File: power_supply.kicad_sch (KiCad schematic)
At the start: 21 parts, among them U3 TPS62913, U4 TPS7A4701RGWR, U5 LDL1117S33R

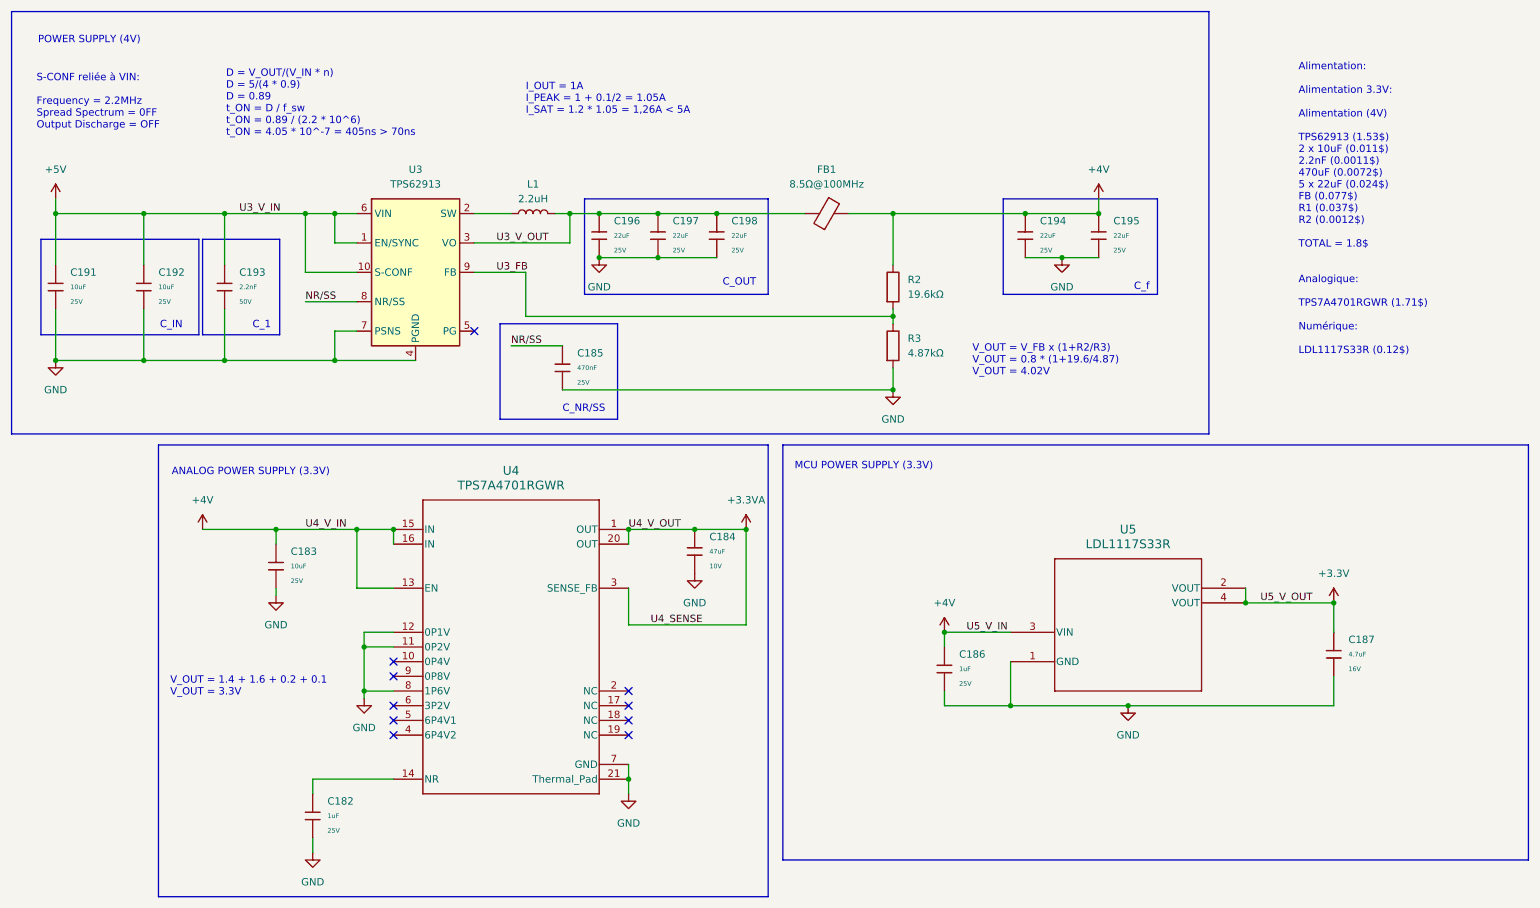
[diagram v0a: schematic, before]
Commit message: start analog ldo layout
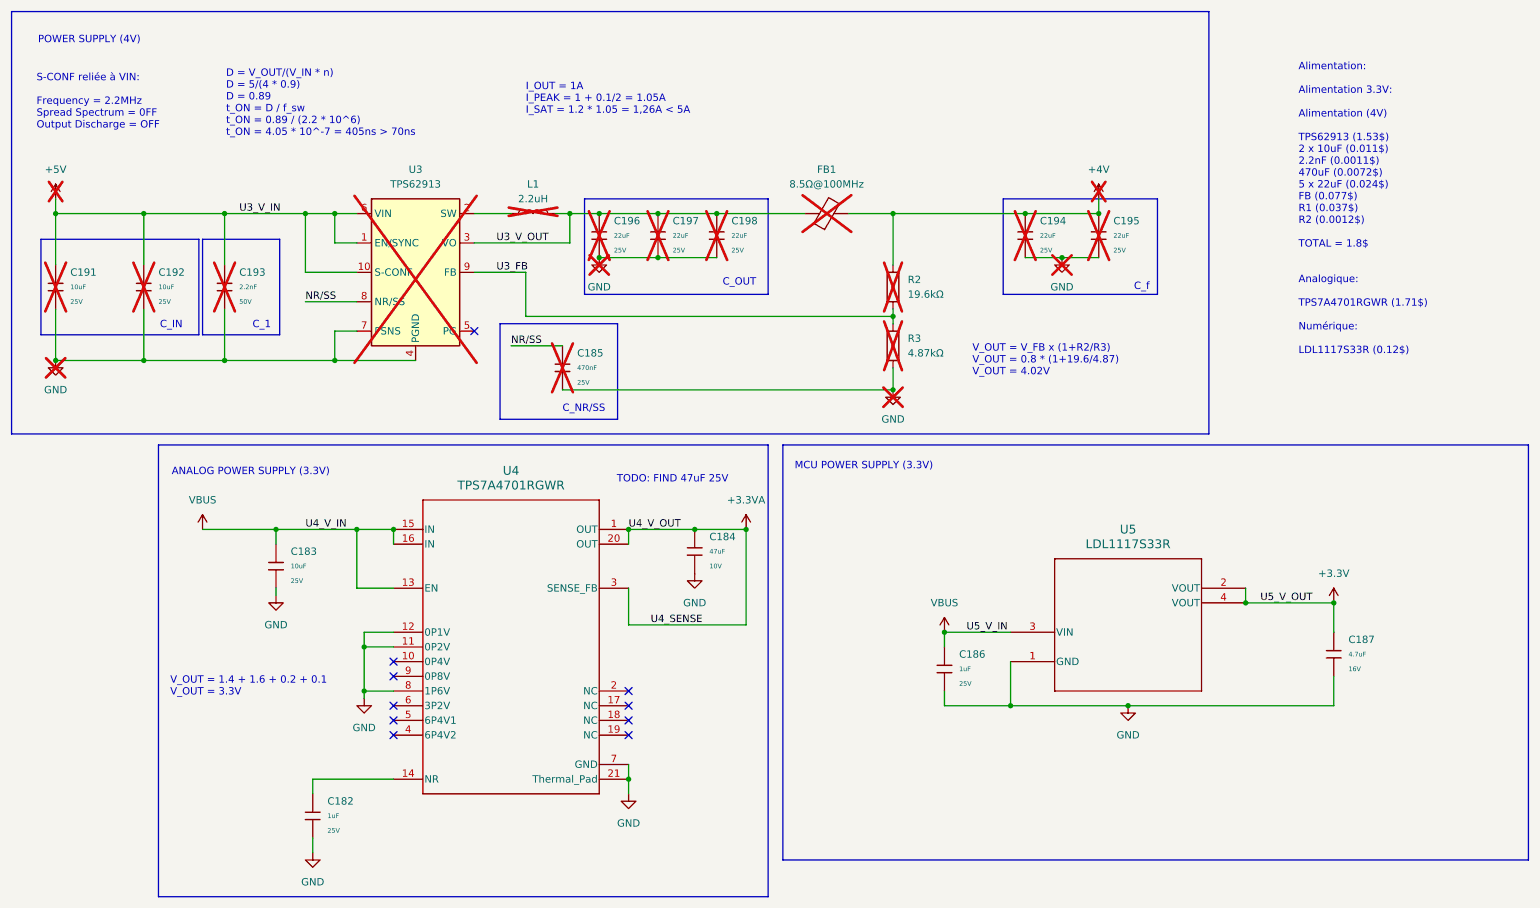
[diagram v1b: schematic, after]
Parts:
- C185, C191, C192, C193, C194, C195, C196, C197, C198, FB1, L1, R2, R3, U3: now not fitted; now left out of the parts list
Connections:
- net +4V: no longer C183.1, C186.1, U4.13 (EN), U4.15 (IN), U4.16 (IN), U5.3 (VIN)
- new net VBUS: C183.1, C186.1, U4.13 (EN), U4.15 (IN), U4.16 (IN), U5.3 (VIN)
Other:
- note added: "TODO: FIND 47uF 25V"

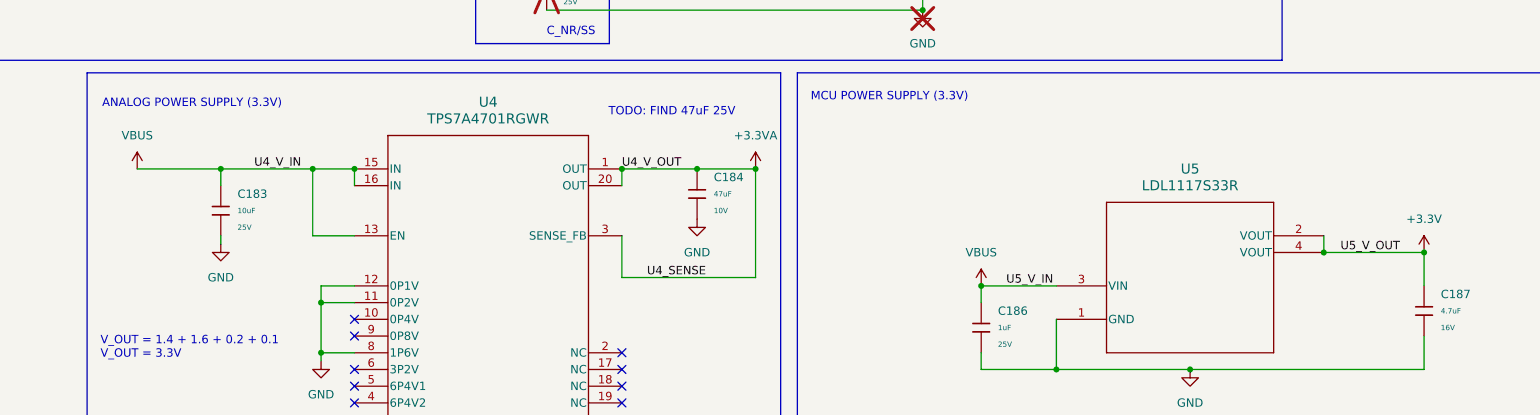
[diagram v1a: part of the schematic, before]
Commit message: vdda power supply & sensor decoupling capacitor
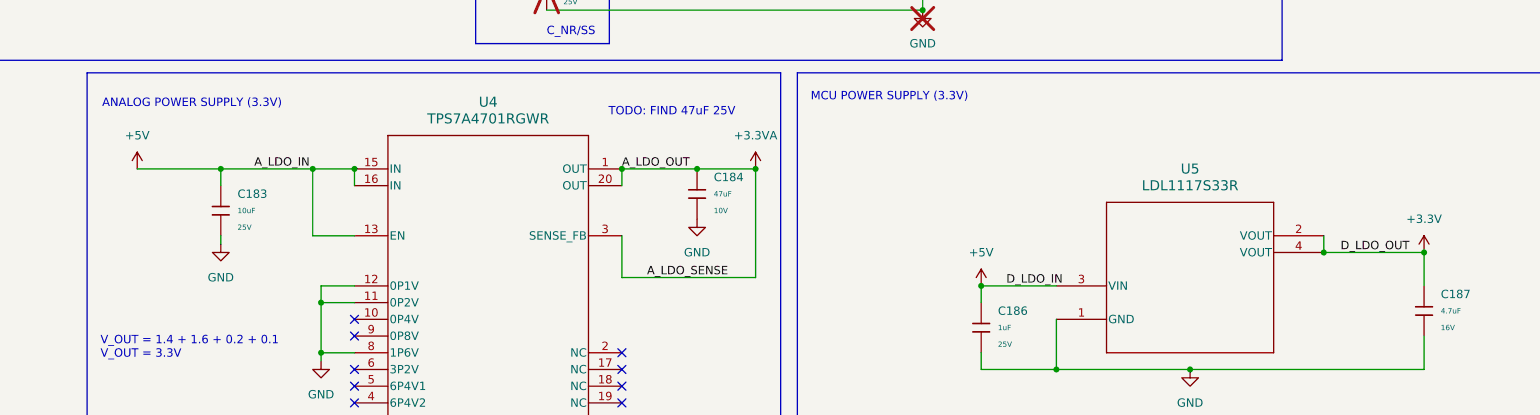
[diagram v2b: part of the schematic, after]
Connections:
- net VBUS is gone; now on net +5V: C183.1, C186.1, U4.13 (EN), U4.15 (IN), U4.16 (IN), U5.3 (VIN)
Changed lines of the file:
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@@
-	)
-	(junction
-		(at 177.8 124.46)
-		(diameter 0)
-		(color 0 0 0 0)
 	)
 	(junction
@@
 	(junction
 		(at 128.27 52.07)
+		(diameter 0)
+		(color 0 0 0 0)
+	)
+	(junction
+		(at 177.8 124.46)
 		(diameter 0)
 		(color 0 0 0 0)
@@
 		)
 	)
-	(label "U4_V_OUT"
+	(label "A_LDO_OUT"
 		(at 123.19 106.68 0)
 		(effects
@@
 		)
 	)
-	(label "U4_V_IN"
+	(label "A_LDO_IN"
 		(at 67.31 106.68 0)
 		(effects
@@
 		)
 	)
-	(label "U4_SENSE"
+	(label "A_LDO_SENSE"
 		(at 127 123.19 0)
 		(effects
@@
 		)
 	)
-	(label "U5_V_OUT"
+	(label "D_LDO_OUT"
 		(at 232.41 119.38 0)
 		(effects
@@
 		)
 	)
-	(label "U5_V_IN"
+	(label "D_LDO_IN"
 		(at 181.61 124.46 0)
 		(effects
@@
 			)
 			(justify left bottom)
-		)
-	)
-	(symbol
-		(lib_id "power:VBUS")
-		(at 177.8 124.46 0)
-		(unit 1)
-		(exclude_from_sim no)
-		(in_bom yes)
-		(on_board yes)
-		(dnp no)
-		(fields_autoplaced yes)
-		(property "Reference" "#PWR0224"
-			(at 177.8 128.27 0)
-			(effects
-				(font
-					(size 1.27 1.27)
-				)
-				(hide yes)
-			)
-		)
-		(property "Value" "VBUS"
-			(at 177.8 119.38 0)
-			(effects
-				(font
-					(size 1.27 1.27)
-				)
-			)
-		)
-		(property "Footprint" ""
-			(at 177.8 124.46 0)
-			(effects
-				(font
-					(size 1.27 1.27)
-				)
-				(hide yes)
-			)
-		)
-		(property "Datasheet" ""
-			(at 177.8 124.46 0)
-			(effects
-				(font
-					(size 1.27 1.27)
-				)
-				(hide yes)
-			)
-		)
-		(property "Description" "Power symbol creates a global label with name \"VBUS\""
-			(at 177.8 124.46 0)
-			(effects
-				(font
-					(size 1.27 1.27)
-				)
-				(hide yes)
-			)
-		)
-		(pin "1"
-		)
-		(instances
-			(project "75he"
-				(path "/0edb4e17-93a4-4f7b-ad91-3a5c72b69d23/f26c38a6-65b7-4d4b-b531-bf41915dd707"
-					(reference "#PWR0224")
-					(unit 1)
-				)
-			)
 		)
 	)
@@
 	)
 	(symbol
+		(lib_id "power:+5V")
+		(at 177.8 124.46 0)
+		(unit 1)
+		(exclude_from_sim no)
+		(in_bom yes)
+		(on_board yes)
+		(dnp no)
+		(fields_autoplaced yes)
+		(property "Reference" "#PWR0223"
+			(at 177.8 128.27 0)
+			(effects
+				(font
+					(size 1.27 1.27)
+				)
+				(hide yes)
+			)
+		)
+		(property "Value" "+5V"
+			(at 177.8 119.38 0)
+			(effects
+				(font
+					(size 1.27 1.27)
+				)
+			)
+		)
+		(property "Footprint" ""
+			(at 177.8 124.46 0)
+			(effects
+				(font
+					(size 1.27 1.27)
+				)
+				(hide yes)
+			)
+		)
+		(property "Datasheet" ""
+			(at 177.8 124.46 0)
+			(effects
+				(font
+					(size 1.27 1.27)
+				)
+				(hide yes)
+			)
+		)
+		(property "Description" "Power symbol creates a global label with name \"+5V\""
+			(at 177.8 124.46 0)
+			(effects
+				(font
+					(size 1.27 1.27)
+				)
+				(hide yes)
+			)
+		)
+		(pin "1"
+		)
+		(instances
+			(project ""
+				(path "/0edb4e17-93a4-4f7b-ad91-3a5c72b69d23/f26c38a6-65b7-4d4b-b531-bf41915dd707"
+					(reference "#PWR0223")
+					(unit 1)
+				)
+			)
+		)
+	)
+	(symbol
 		(lib_id "Device:R")
 		(at 168.91 74.93 0)
@@
 	)
 	(symbol
+		(lib_id "power:+5V")
+		(at 49.53 106.68 0)
+		(unit 1)
+		(exclude_from_sim no)
+		(in_bom yes)
+		(on_board yes)
+		(dnp no)
+		(fields_autoplaced yes)
+		(property "Reference" "#PWR0221"
+			(at 49.53 110.49 0)
+			(effects
+				(font
+					(size 1.27 1.27)
+				)
+				(hide yes)
+			)
+		)
+		(property "Value" "+5V"
+			(at 49.53 101.6 0)
+			(effects
+				(font
+					(size 1.27 1.27)
+				)
+			)
+		)
+		(property "Footprint" ""
+			(at 49.53 106.68 0)
+			(effects
+				(font
+					(size 1.27 1.27)
+				)
+				(hide yes)
+			)
+		)
+		(property "Datasheet" ""
+			(at 49.53 106.68 0)
+			(effects
+				(font
+					(size 1.27 1.27)
+				)
+				(hide yes)
+			)
+		)
+		(property "Description" "Power symbol creates a global label with name \"+5V\""
+			(at 49.53 106.68 0)
+			(effects
+				(font
+					(size 1.27 1.27)
+				)
+				(hide yes)
+			)
+		)
+		(pin "1"
+		)
+		(instances
+			(project ""
+				(path "/0edb4e17-93a4-4f7b-ad91-3a5c72b69d23/f26c38a6-65b7-4d4b-b531-bf41915dd707"
+					(reference "#PWR0221")
+					(unit 1)
+				)
+			)
+		)
+	)
+	(symbol
 		(lib_id "Device:L")
 		(at 106.68 52.07 90)
@@
 					(unit 1)
 				)
-			)
-		)
-	)
-	(symbol
-		(lib_id "power:VBUS")
-		(at 49.53 106.68 0)
-		(unit 1)
-		(exclude_from_sim no)
-		(in_bom yes)
-		(on_board yes)
-		(dnp no)
-		(fields_autoplaced yes)
-		(property "Reference" "#PWR0223"
-			(at 49.53 110.49 0)
-			(effects
-				(font
-					(size 1.27 1.27)
-				)
-				(hide yes)
-			)
-		)
-		(property "Value" "VBUS"
-			(at 49.53 101.6 0)
-			(effects
-				(font
-					(size 1.27 1.27)
-				)
-			)
-		)
-		(property "Footprint" ""
-			(at 49.53 106.68 0)
-			(effects
-				(font
-					(size 1.27 1.27)
-				)
-				(hide yes)
-			)
-		)
-		(property "Datasheet" ""
-			(at 49.53 106.68 0)
-			(effects
-				(font
-					(size 1.27 1.27)
-				)
-				(hide yes)
-			)
-		)
-		(property "Description" "Power symbol creates a global label with name \"VBUS\""
-			(at 49.53 106.68 0)
-			(effects
-				(font
-					(size 1.27 1.27)
-				)
-				(hide yes)
-			)
-		)
-		(pin "1"
-		)
-		(instances
-			(project ""
-				(path "/0edb4e17-93a4-4f7b-ad91-3a5c72b69d23/f26c38a6-65b7-4d4b-b531-bf41915dd707"
-					(reference "#PWR0223")
-					(unit 1)
-				)

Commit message: caca
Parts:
- removed C185: 470nF, PCM_JLCPCB:C_0603, symbol PCM_JLCPCB-Capacitors:0603,470nF
- removed C191, C192: 10uF, PCM_JLCPCB:C_0805, symbol PCM_JLCPCB-Capacitors:0805,10uF
- removed C193: 2.2nF, PCM_JLCPCB:C_0402, symbol PCM_JLCPCB-Capacitors:0402,2.2nF
- removed C194, C195, C196, C197, C198: 22uF, PCM_JLCPCB:C_0805, symbol PCM_JLCPCB-Capacitors:0805,22uF
- removed FB1: 8.5Ω@100MHz, PCM_JLCPCB:FB_0603, symbol Device:FerriteBead
- removed L1: 2.2uH, Inductor_SMD:L_1210_3225Metric, symbol Device:L
- removed R2: 19.6kΩ, Resistor_SMD:R_0402_1005Metric, symbol Device:R
- removed R3: 4.87kΩ, PCM_JLCPCB:R_0603, symbol Device:R
- removed U3: TPS62913, Package_DFN_QFN:Texas_RPU0010A_VQFN-HR-10_2x2mm_P0.5mm, symbol Regulator_Switching:TPS62913
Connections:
- no-connect marks 10 -> 9
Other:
- note removed: "C_1"
- note removed: "C_IN"
- note removed: "C_NR/SS"
- note removed: "C_OUT"
- note removed: "C_f"
- note removed: "D = V_OUT/(V_IN * n) D = 5/(4 * 0.9) D = 0.89 t_ON = D / f_sw t_ON = 0.89 / (2.2 * 10^6) t_ON = 4.05 * 10^-7 = 405ns > 70ns"
- note removed: "I_OUT = 1A I_PEAK = 1 + 0.1/2 = 1.05A I_SAT = 1.2 * 1.05 = 1,26A < 5A"
- note removed: "POWER SUPPLY (4V)"
- note removed: "S-CONF reliée à VIN: Frequency = 2.2MHz Spread Spectrum = 0FF Output Discharge = OFF"
- note removed: "V_OUT = V_FB x (1+R2/R3) V_OUT = 0.8 * (1+19.6/4.87) V_OUT = 4.02V"

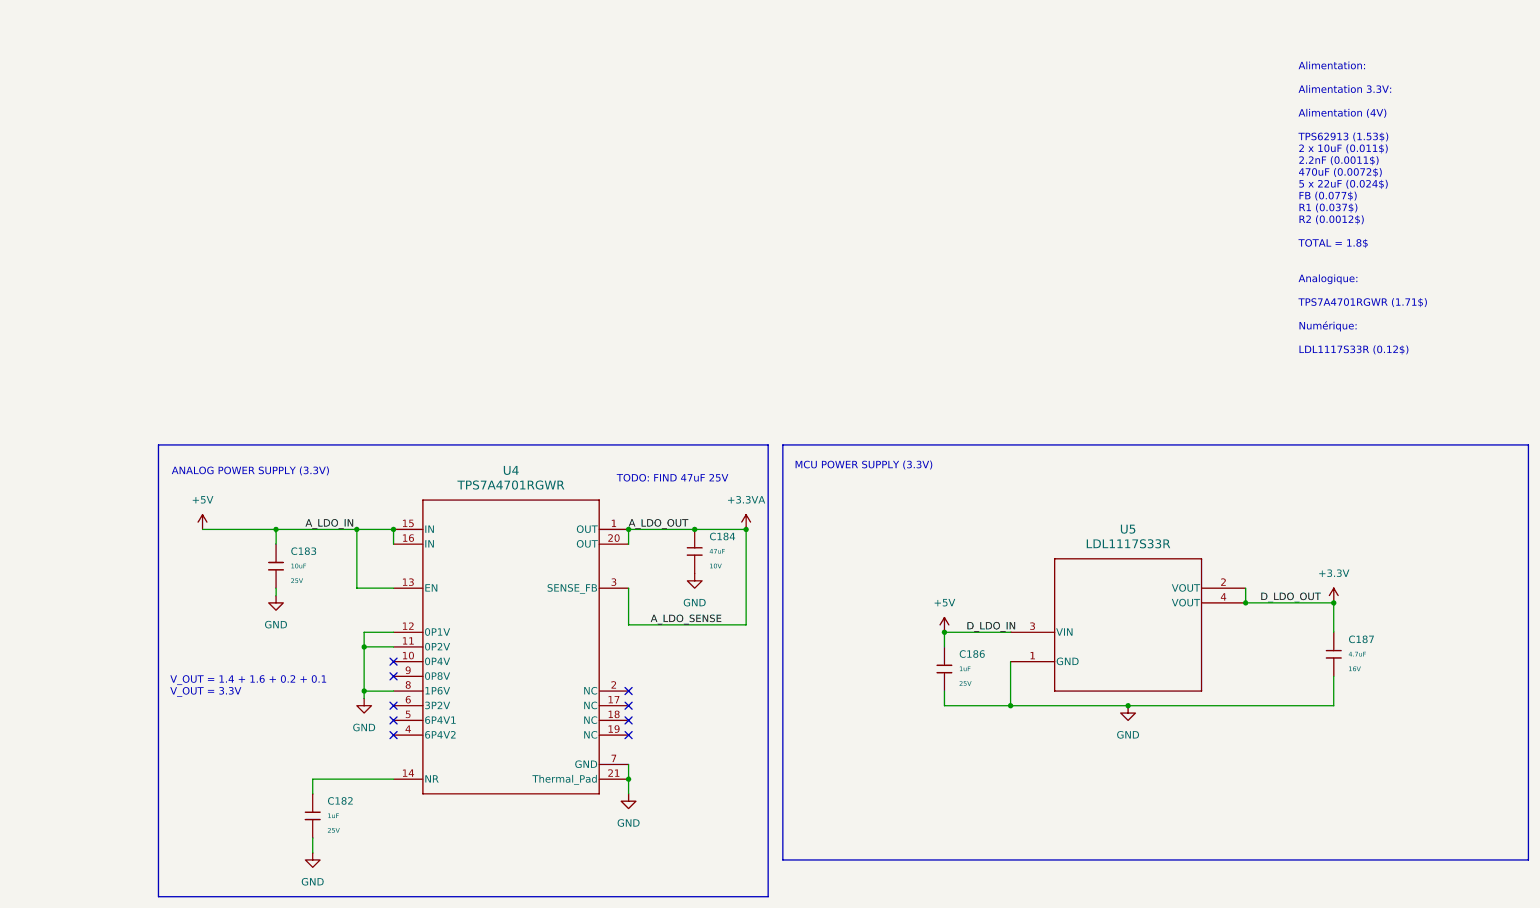
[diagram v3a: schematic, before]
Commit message: added power led, some cleanup/fixes, added doc
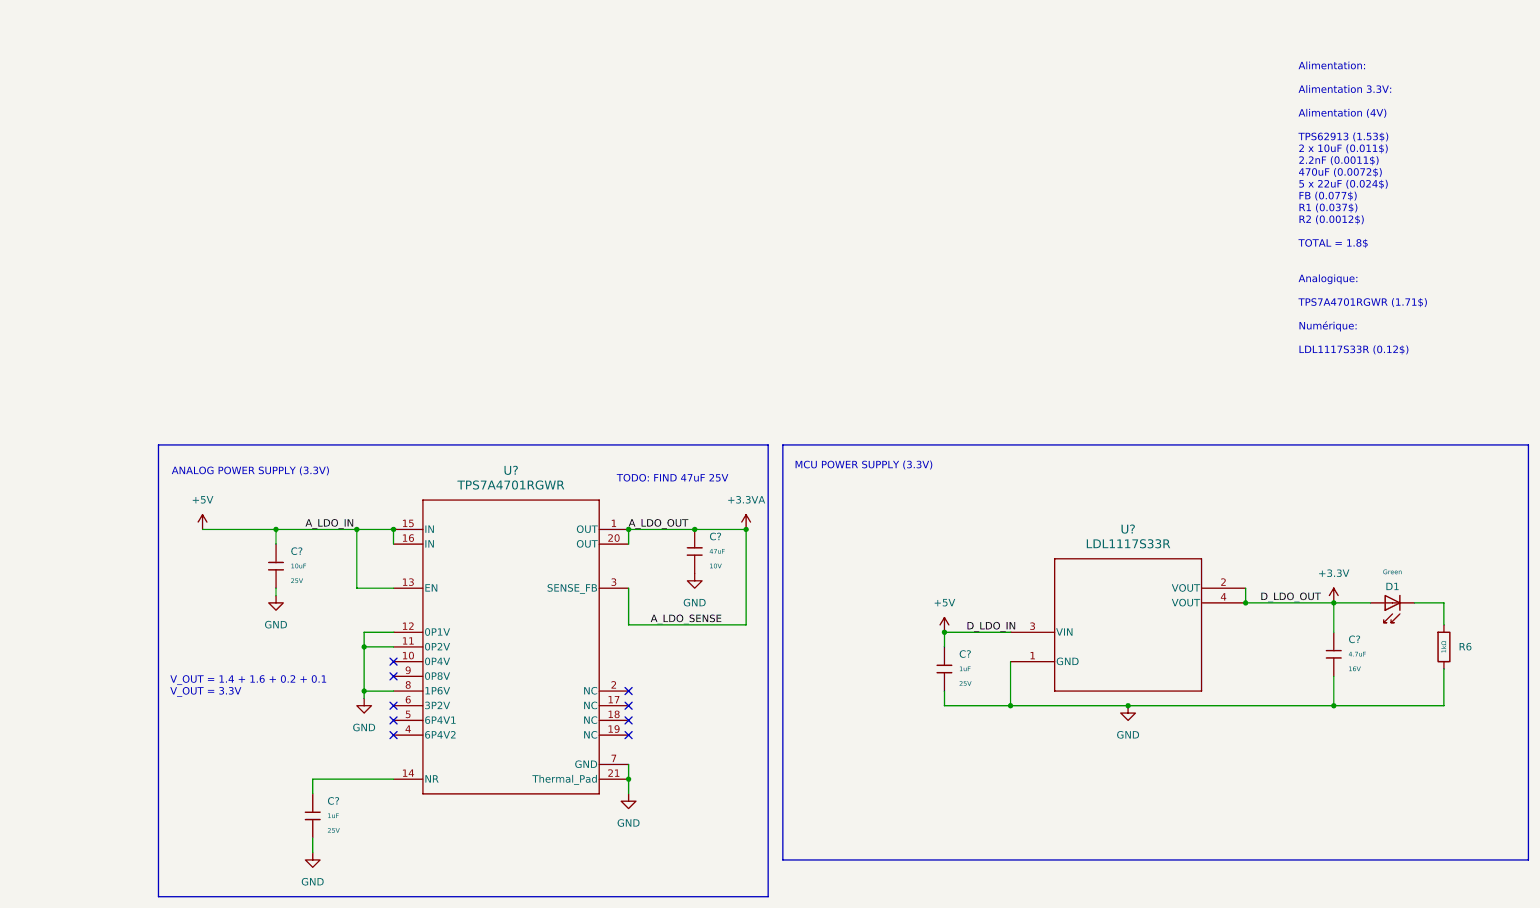
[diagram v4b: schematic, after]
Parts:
- added D1: Green, PCM_JLCPCB:D_0805, symbol PCM_JLCPCB-Diodes:LED,0805,Green
- added R6: 1kΩ, PCM_JLCPCB:R_0402, symbol PCM_JLCPCB-Resistors:0402,1kΩ
- renumbered C184 to C?, C182 to C?, C187 to C?, C183 to C?, C186 to C?, U5 to U?, U4 to U?
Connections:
- net +3.3V: now also D1.2
- net GND: now also R6.2
- new net: D1.1, R6.1
